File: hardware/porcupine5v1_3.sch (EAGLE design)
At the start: 45 parts, among them X1 PROGCON

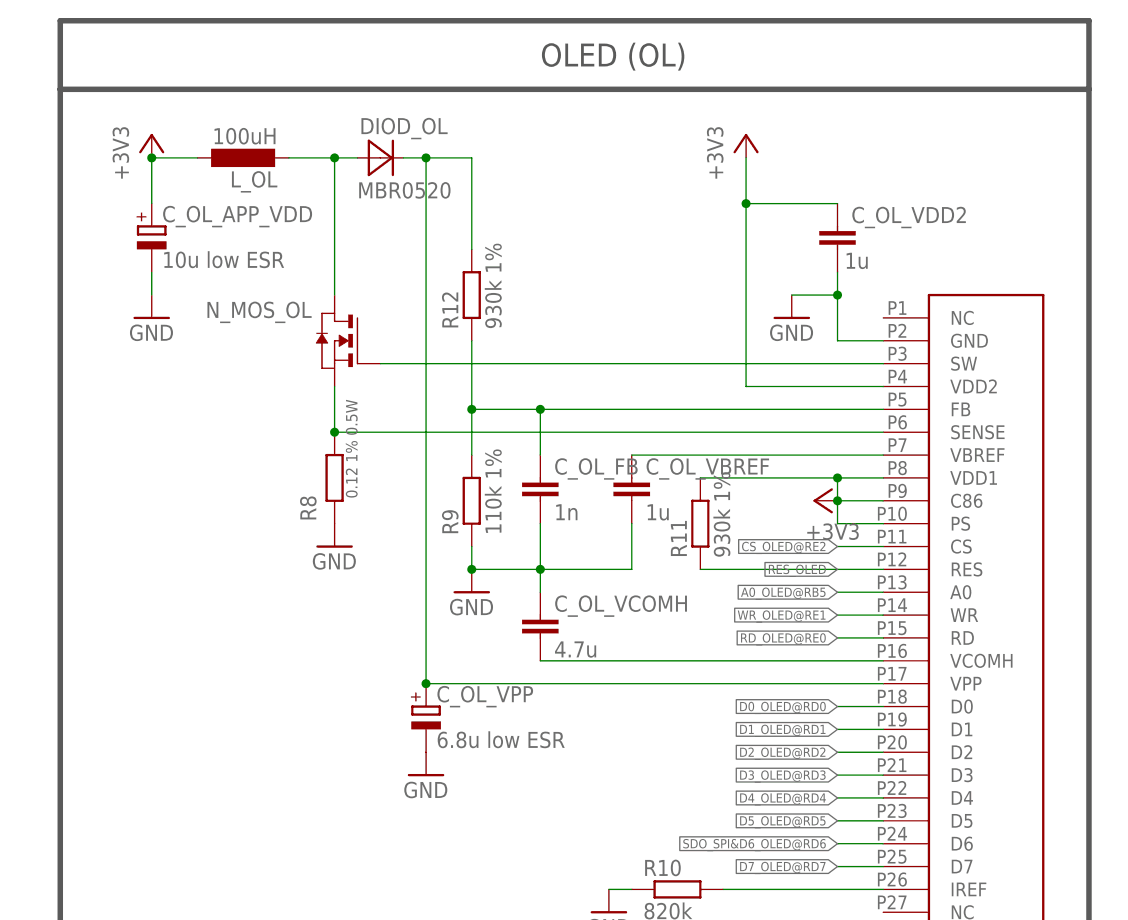
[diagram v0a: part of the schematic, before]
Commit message: OLED version: a) updating coil eagle package b) fixing BOM list (resistors)
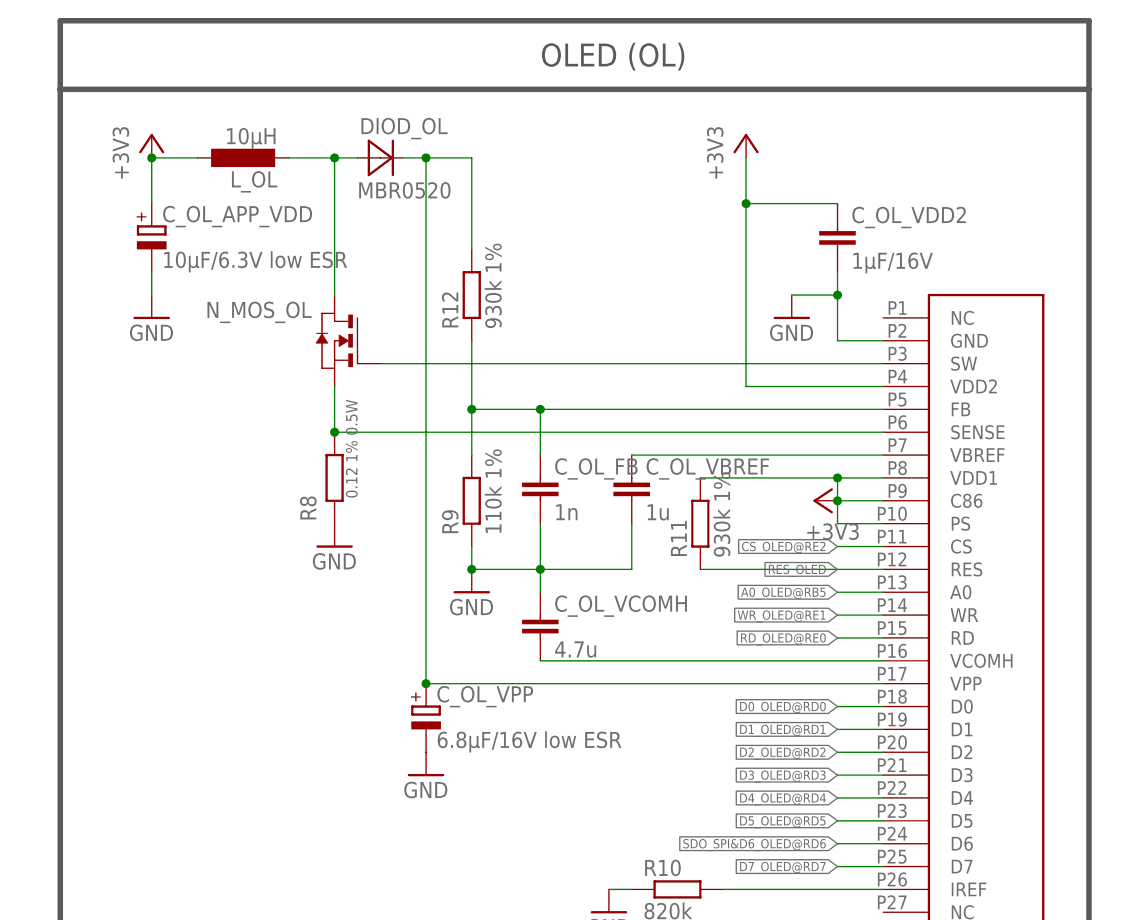
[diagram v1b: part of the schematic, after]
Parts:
- C_OL_APP_VDD: value 10u low ESR -> 10µF/6.3V low ESR
- C_OL_VDD2: value 1u -> 1µF/16V
- C_OL_VPP: value 6.8u low ESR -> 6.8µF/16V low ESR
- L_OL: value 100uH -> 10µH
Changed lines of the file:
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@@
 <part name="CON_OLED" library="HedgehogLib" deviceset="OLED_DENSITRON" device=""/>
 <part name="DIOD_OL" library="HedgehogLib" deviceset="MBR0520" device=""/>
-<part name="L_OL" library="HedgehogLib" deviceset="LQH3NP" device="" value="100uH"/>
+<part name="L_OL" library="HedgehogLib" deviceset="LQH3NP" device="" value="10µH"/>
 <part name="GND1" library="supply1" deviceset="GND" device=""/>
-<part name="C_OL_APP_VDD" library="rcl" deviceset="CPOL-EU" device="A/3216-18R" value="10u low ESR"/>
+<part name="C_OL_APP_VDD" library="rcl" deviceset="CPOL-EU" device="A/3216-18R" value="10µF/6.3V low ESR"/>
 <part name="R12" library="rcl" deviceset="R-EU_" device="R0603" value="930k 1%"/>
 <part name="R9" library="rcl" deviceset="R-EU_" device="R0603" value="110k 1%"/>
-<part name="C_OL_VPP" library="rcl" deviceset="CPOL-EU" device="A/3216-18R" value="6.8u low ESR"/>
+<part name="C_OL_VPP" library="rcl" deviceset="CPOL-EU" device="A/3216-18R" value="6.8µF/16V low ESR"/>
 <part name="C_OL_FB" library="rcl" deviceset="C-EU" device="C0603K" value="1n"/>
 <part name="GND8" library="supply1" deviceset="GND" device=""/>
@@
 <part name="GND12" library="supply1" deviceset="GND" device=""/>
 <part name="C_OL_VBREF" library="rcl" deviceset="C-EU" device="C0603K" value="1u"/>
-<part name="C_OL_VDD2" library="rcl" deviceset="C-EU" device="C0603K" value="1u"/>
+<part name="C_OL_VDD2" library="rcl" deviceset="C-EU" device="C0603K" value="1µF/16V"/>
 <part name="GND14" library="supply1" deviceset="GND" device=""/>
 <part name="C_OL_VCOMH" library="rcl" deviceset="C-EU" device="C0603K" value="4.7u"/>
@@
 <instance part="C_OL_VDD2" gate="G$1" x="284.48" y="210.82" smashed="yes" rot="R180">
 <attribute name="NAME" x="286.004" y="213.741" size="1.778" layer="95"/>
-<attribute name="VALUE" x="288.036" y="210.439" size="1.778" layer="96" rot="R180"/>
+<attribute name="VALUE" x="286.004" y="208.661" size="1.778" layer="96"/>
 </instance>
 <instance part="GND14" gate="1" x="279.4" y="203.2"/>

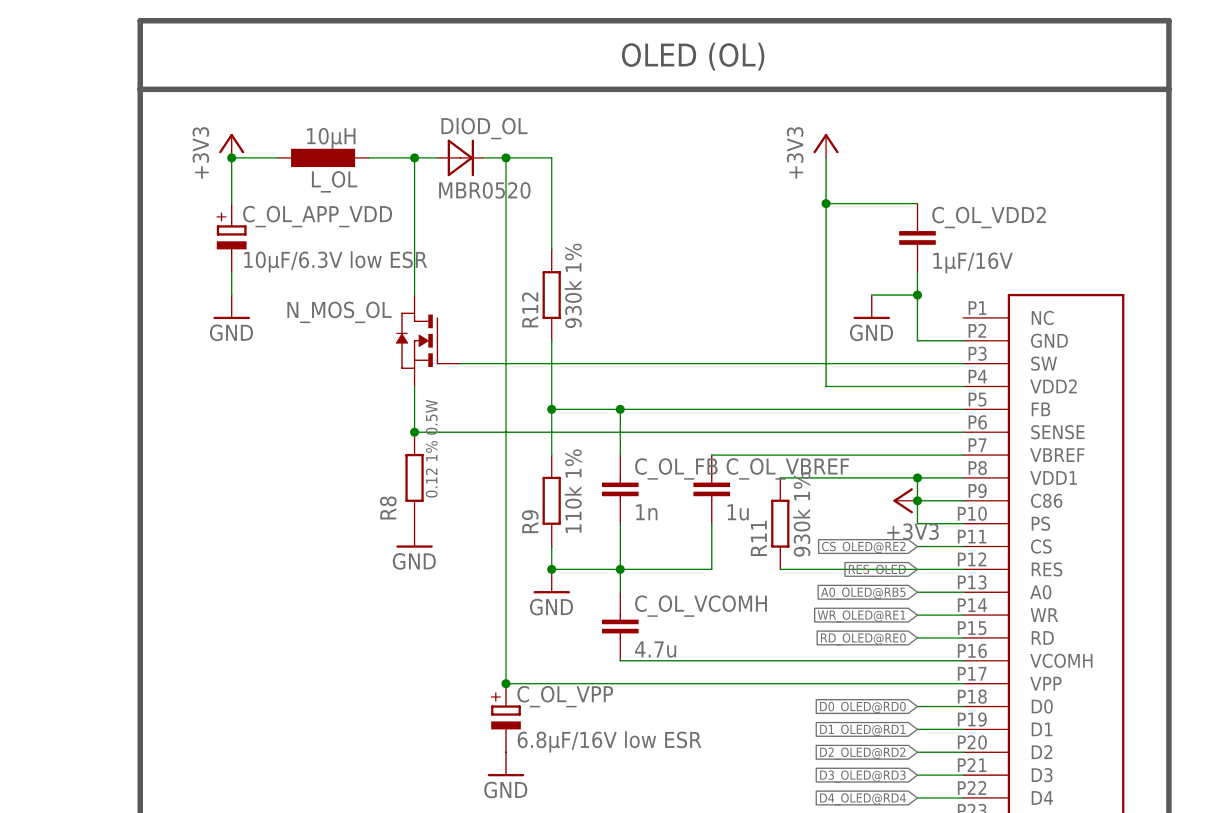
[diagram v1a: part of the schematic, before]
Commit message: OLED version: improved eagle schematics
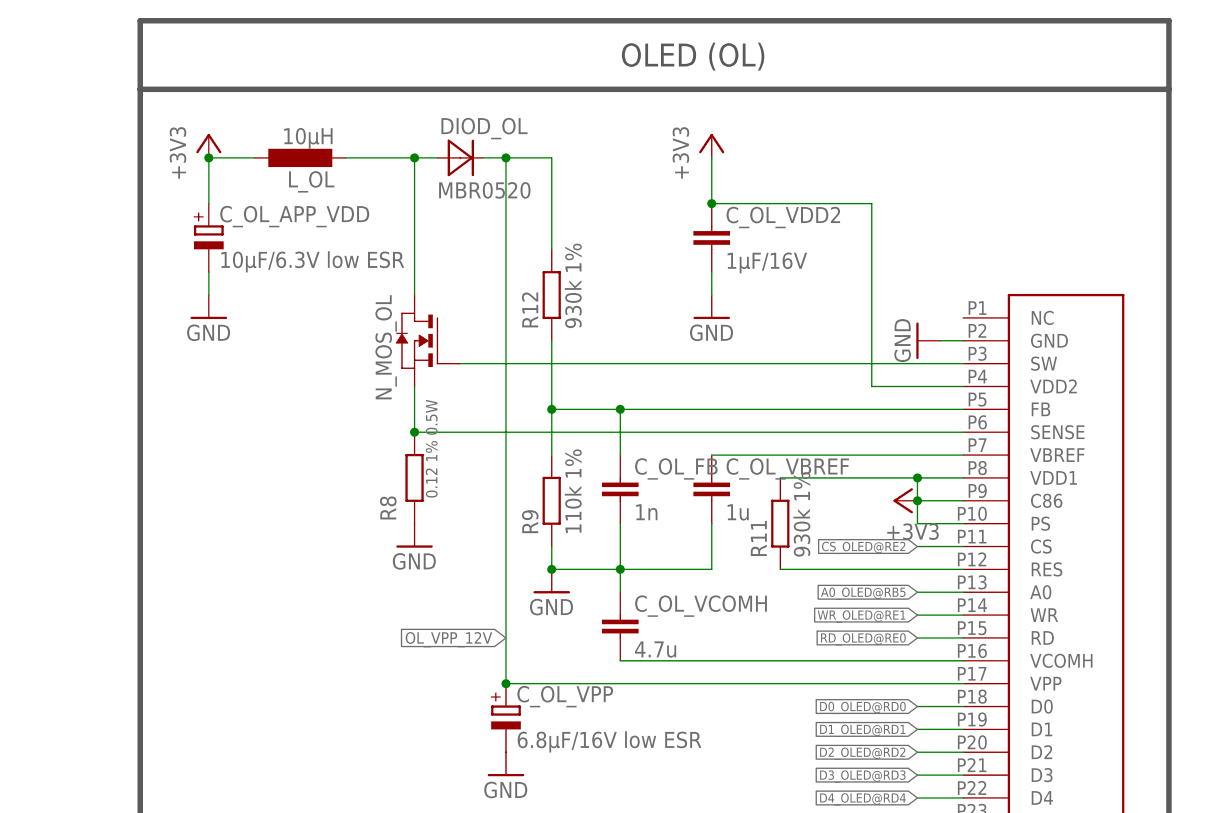
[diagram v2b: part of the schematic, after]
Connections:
- net N$11 renamed OL_SW
- net N$12 renamed OL_VPP_12V
- net N$13 renamed OL_SENSE
- net N$15 renamed OL_FB
- net N$18 renamed OL_VBREF
- net N$21 renamed OL_VCOMH
- net N$30 renamed OL_IREF
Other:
- moved on the sheet: C_OL_APP_VDD, C_OL_VDD2, L_OL
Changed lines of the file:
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@@
 <?xml version="1.0" encoding="utf-8"?>
 <!DOCTYPE eagle SYSTEM "eagle.dtd">
-<eagle version="6.5.0">
+<eagle version="6.4">
 <drawing>
 <settings>
@@
 <part name="BAT" library="con-molex" deviceset="53?-02" device="048"/>
 <part name="R7" library="rcl" deviceset="R-EU_" device="R0603" value="10k"/>
+<part name="GND18" library="supply1" deviceset="GND" device=""/>
 </parts>
 <sheets>
@@
 <instance part="CON_OLED" gate="G$1" x="292.1" y="170.18"/>
 <instance part="DIOD_OL" gate="G$1" x="233.68" y="220.98"/>
-<instance part="L_OL" gate="G$1" x="218.44" y="220.98" rot="R90"/>
+<instance part="L_OL" gate="G$1" x="215.9" y="220.98" rot="R90"/>
 <instance part="GND1" gate="1" x="228.6" y="177.8"/>
-<instance part="C_OL_APP_VDD" gate="G$1" x="208.28" y="213.36"/>
+<instance part="C_OL_APP_VDD" gate="G$1" x="205.74" y="213.36"/>
 <instance part="R12" gate="G$1" x="243.84" y="205.74" rot="R90"/>
 <instance part="R9" gate="G$1" x="243.84" y="182.88" rot="R90"/>
@@
 <instance part="GND8" gate="1" x="243.84" y="172.72"/>
 <instance part="GND10" gate="1" x="238.76" y="152.4"/>
-<instance part="GND12" gate="1" x="208.28" y="203.2"/>
+<instance part="GND12" gate="1" x="205.74" y="203.2"/>
 <instance part="C_OL_VBREF" gate="G$1" x="261.62" y="185.42"/>
-<instance part="C_OL_VDD2" gate="G$1" x="284.48" y="210.82" smashed="yes" rot="R180">
-<attribute name="NAME" x="286.004" y="213.741" size="1.778" layer="95"/>
-<attribute name="VALUE" x="286.004" y="208.661" size="1.778" layer="96"/>
+<instance part="C_OL_VDD2" gate="G$1" x="261.62" y="210.82" smashed="yes" rot="R180">
+<attribute name="NAME" x="263.144" y="213.741" size="1.778" layer="95"/>
+<attribute name="VALUE" x="263.144" y="208.661" size="1.778" layer="96"/>
 </instance>
-<instance part="GND14" gate="1" x="279.4" y="203.2"/>
+<instance part="GND14" gate="1" x="261.62" y="203.2"/>
 <instance part="C_OL_VCOMH" gate="G$1" x="251.46" y="170.18"/>
 <instance part="R10" gate="G$1" x="266.7" y="139.7"/>
 <instance part="GND15" gate="1" x="259.08" y="137.16"/>
-<instance part="+3V17" gate="G$1" x="208.28" y="223.52"/>
-<instance part="+3V18" gate="G$1" x="274.32" y="223.52"/>
+<instance part="+3V17" gate="G$1" x="205.74" y="223.52"/>
+<instance part="+3V18" gate="G$1" x="261.62" y="223.52"/>
 <instance part="+3V19" gate="G$1" x="281.94" y="182.88" rot="R90"/>
 <instance part="X1" gate="-1" x="38.1" y="142.24" smashed="yes">
@@
 <instance part="R11" gate="G$1" x="269.24" y="180.34" rot="R90"/>
 <instance part="R8" gate="G$1" x="228.6" y="185.42" rot="R90"/>
-<instance part="N_MOS_OL" gate="A" x="228.6" y="200.66" rot="MR0"/>
+<instance part="N_MOS_OL" gate="A" x="228.6" y="200.66" smashed="yes" rot="MR0">
+<attribute name="VALUE" x="226.06" y="200.66" size="1.778" layer="96" rot="MR0"/>
+<attribute name="NAME" x="226.06" y="205.74" size="1.778" layer="95" rot="MR270"/>
+</instance>
 <instance part="LDO" gate="LDO" x="139.7" y="93.98"/>
 <instance part="R3" gate="G$1" x="68.58" y="109.22" rot="R90"/>
@@
 <instance part="BAT" gate="-2" x="91.44" y="116.84" rot="R180"/>
 <instance part="R7" gate="G$1" x="76.2" y="149.86" rot="R90"/>
+<instance part="GND18" gate="1" x="284.48" y="200.66" rot="R270"/>
 </instances>
 <busses>
@@
 </segment>
 <segment>
-<wire x1="208.28" y1="205.74" x2="208.28" y2="208.28" width="0.1524" layer="91"/>
 <pinref part="C_OL_APP_VDD" gate="G$1" pin="-"/>
 <pinref part="GND12" gate="1" pin="GND"/>
-</segment>
-<segment>
-<wire x1="289.56" y1="200.66" x2="284.48" y2="200.66" width="0.1524" layer="91"/>
-<wire x1="284.48" y1="200.66" x2="284.48" y2="205.74" width="0.1524" layer="91"/>
-<wire x1="284.48" y1="208.28" x2="284.48" y2="205.74" width="0.1524" layer="91"/>
-<wire x1="284.48" y1="205.74" x2="279.4" y2="205.74" width="0.1524" layer="91"/>
-<junction x="284.48" y="205.74"/>
-<pinref part="CON_OLED" gate="G$1" pin="GND"/>
+<wire x1="205.74" y1="205.74" x2="205.74" y2="208.28" width="0.1524" layer="91"/>
+</segment>
+<segment>
 <pinref part="C_OL_VDD2" gate="G$1" pin="1"/>
 <pinref part="GND14" gate="1" pin="GND"/>
+<wire x1="261.62" y1="208.28" x2="261.62" y2="205.74" width="0.1524" layer="91"/>
 </segment>
 <segment>
@@
 <pinref part="BAT" gate="-2" pin="S"/>
 <wire x1="96.52" y1="116.84" x2="93.98" y2="116.84" width="0.1524" layer="91"/>
+</segment>
+<segment>
+<pinref part="CON_OLED" gate="G$1" pin="GND"/>
+<pinref part="GND18" gate="1" pin="GND"/>
+<wire x1="287.02" y1="200.66" x2="289.56" y2="200.66" width="0.1524" layer="91"/>
 </segment>
 </net>
@@
 </segment>
 <segment>
-<wire x1="213.36" y1="220.98" x2="208.28" y2="220.98" width="0.1524" layer="91"/>
-<wire x1="208.28" y1="220.98" x2="208.28" y2="215.9" width="0.1524" layer="91"/>
-<junction x="208.28" y="220.98"/>
+<wire x1="210.82" y1="220.98" x2="205.74" y2="220.98" width="0.1524" layer="91"/>
+<wire x1="205.74" y1="220.98" x2="205.74" y2="215.9" width="0.1524" layer="91"/>
+<junction x="205.74" y="220.98"/>
 <pinref part="L_OL" gate="G$1" pin="1"/>
 <pinref part="C_OL_APP_VDD" gate="G$1" pin="+"/>
@@
 </segment>
 <segment>
-<wire x1="289.56" y1="195.58" x2="274.32" y2="195.58" width="0.1524" layer="91"/>
-<wire x1="274.32" y1="195.58" x2="274.32" y2="215.9" width="0.1524" layer="91"/>
-<wire x1="274.32" y1="220.98" x2="274.32" y2="215.9" width="0.1524" layer="91"/>
-<wire x1="274.32" y1="215.9" x2="284.48" y2="215.9" width="0.1524" layer="91"/>
-<junction x="274.32" y="215.9"/>
+<wire x1="289.56" y1="195.58" x2="279.4" y2="195.58" width="0.1524" layer="91"/>
+<wire x1="279.4" y1="195.58" x2="279.4" y2="215.9" width="0.1524" layer="91"/>
+<wire x1="279.4" y1="215.9" x2="261.62" y2="215.9" width="0.1524" layer="91"/>
+<wire x1="261.62" y1="220.98" x2="261.62" y2="215.9" width="0.1524" layer="91"/>
+<junction x="261.62" y="215.9"/>
 <pinref part="CON_OLED" gate="G$1" pin="VDD2"/>
 <pinref part="C_OL_VDD2" gate="G$1" pin="2"/>
@@
 <wire x1="228.6" y1="205.74" x2="228.6" y2="220.98" width="0.1524" layer="91"/>
 <wire x1="228.6" y1="220.98" x2="231.14" y2="220.98" width="0.1524" layer="91"/>
-<wire x1="228.6" y1="220.98" x2="223.52" y2="220.98" width="0.1524" layer="91"/>
+<wire x1="228.6" y1="220.98" x2="220.98" y2="220.98" width="0.1524" layer="91"/>
 <junction x="228.6" y="220.98"/>
 <pinref part="DIOD_OL" gate="G$1" pin="A"/>
@@
 </segment>
 </net>
-<net name="N$11" class="0">
+<net name="OL_SW" class="0">
 <segment>
 <wire x1="289.56" y1="198.12" x2="233.68" y2="198.12" width="0.1524" layer="91"/>
@@
 </segment>
 </net>
-<net name="N$12" class="0">
+<net name="OL_VPP_12V" class="0">
 <segment>
 <wire x1="236.22" y1="220.98" x2="238.76" y2="220.98" width="0.1524" layer="91"/>
@@
 <pinref part="R12" gate="G$1" pin="2"/>
 <pinref part="C_OL_VPP" gate="G$1" pin="+"/>
-</segment>
-</net>
-<net name="N$13" class="0">
+<label x="238.76" y="167.64" size="1.27" layer="95" rot="R180" xref="yes"/>
+</segment>
+</net>
+<net name="OL_SENSE" class="0">
 <segment>
 <wire x1="289.56" y1="190.5" x2="228.6" y2="190.5" width="0.1524" layer="91"/>
@@
 </segment>
 </net>
-<net name="N$15" class="0">
+<net name="OL_FB" class="0">
 <segment>
 <wire x1="289.56" y1="193.04" x2="251.46" y2="193.04" width="0.1524" layer="91"/>
@@
 </segment>
 </net>
-<net name="N$18" class="0">
+<net name="OL_VBREF" class="0">
 <segment>
 <wire x1="289.56" y1="187.96" x2="261.62" y2="187.96" width="0.1524" layer="91"/>
@@
 <segment>
 <wire x1="289.56" y1="175.26" x2="269.24" y2="175.26" width="0.1524" layer="91"/>
-<label x="284.48" y="175.26" size="1.016" layer="95" rot="R180" xref="yes"/>
 <pinref part="CON_OLED" gate="G$1" pin="RES"/>
 <pinref part="R11" gate="G$1" pin="1"/>
@@
 </segment>
 </net>
-<net name="N$21" class="0">
+<net name="OL_VCOMH" class="0">
 <segment>
 <wire x1="251.46" y1="165.1" x2="289.56" y2="165.1" width="0.1524" layer="91"/>
@@
 </segment>
 </net>
-<net name="N$30" class="0">
+<net name="OL_IREF" class="0">
 <segment>
 <wire x1="289.56" y1="139.7" x2="271.78" y2="139.7" width="0.1524" layer="91"/>
